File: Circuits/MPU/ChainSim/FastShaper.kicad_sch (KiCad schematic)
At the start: 34 parts, among them U20 ADA4805-2ARMZ, U21 ADA4805-2ARMZ

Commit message: sim snapshot
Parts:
- renumbered C79 to C1, C88 to C10, C89 to C11, C90 to C12, C80 to C2, C81 to C3, C82 to C4, C83 to C5, C84 to C6, C85 to C7, C86 to C8, C87 to C9, D19 to D1, D20 to D2, R112 to R10, R113 to R11, R114 to R12, R115 to R13, R116 to R14, R117 to R15, R118 to R16, R119 to R17, R120 to R18, R121 to R19, R122 to R20, R105 to R3, R106 to R4, R107 to R5, R108 to R6, R109 to R7, R110 to R8, R111 to R9, U20 to U3, U21 to U4

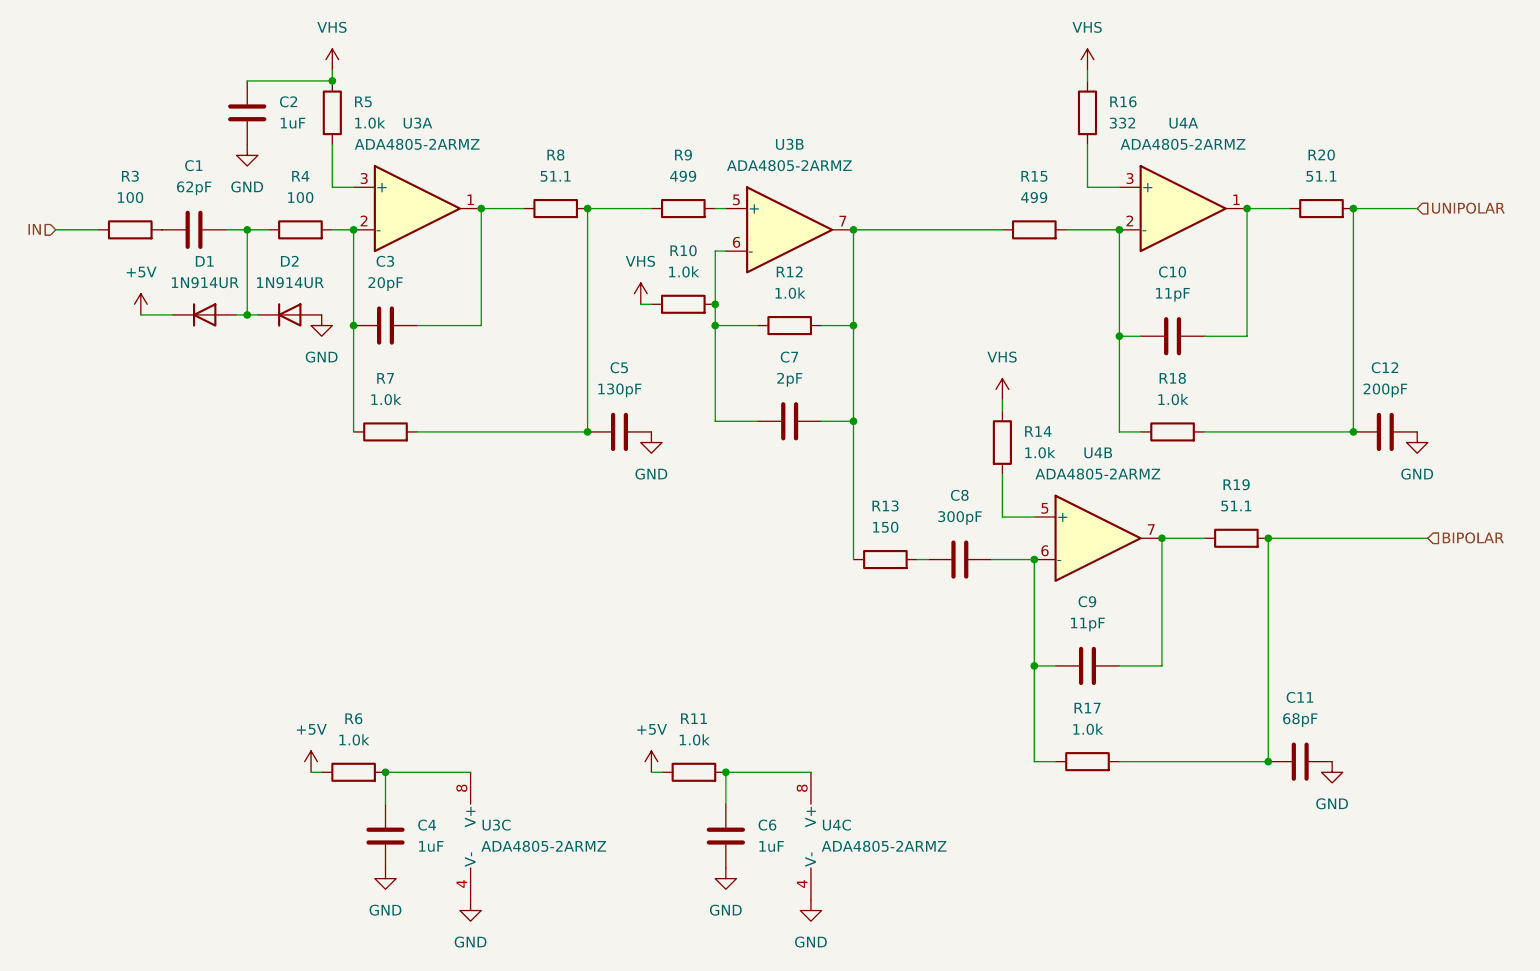
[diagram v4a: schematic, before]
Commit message: exported netlist works with ngspice
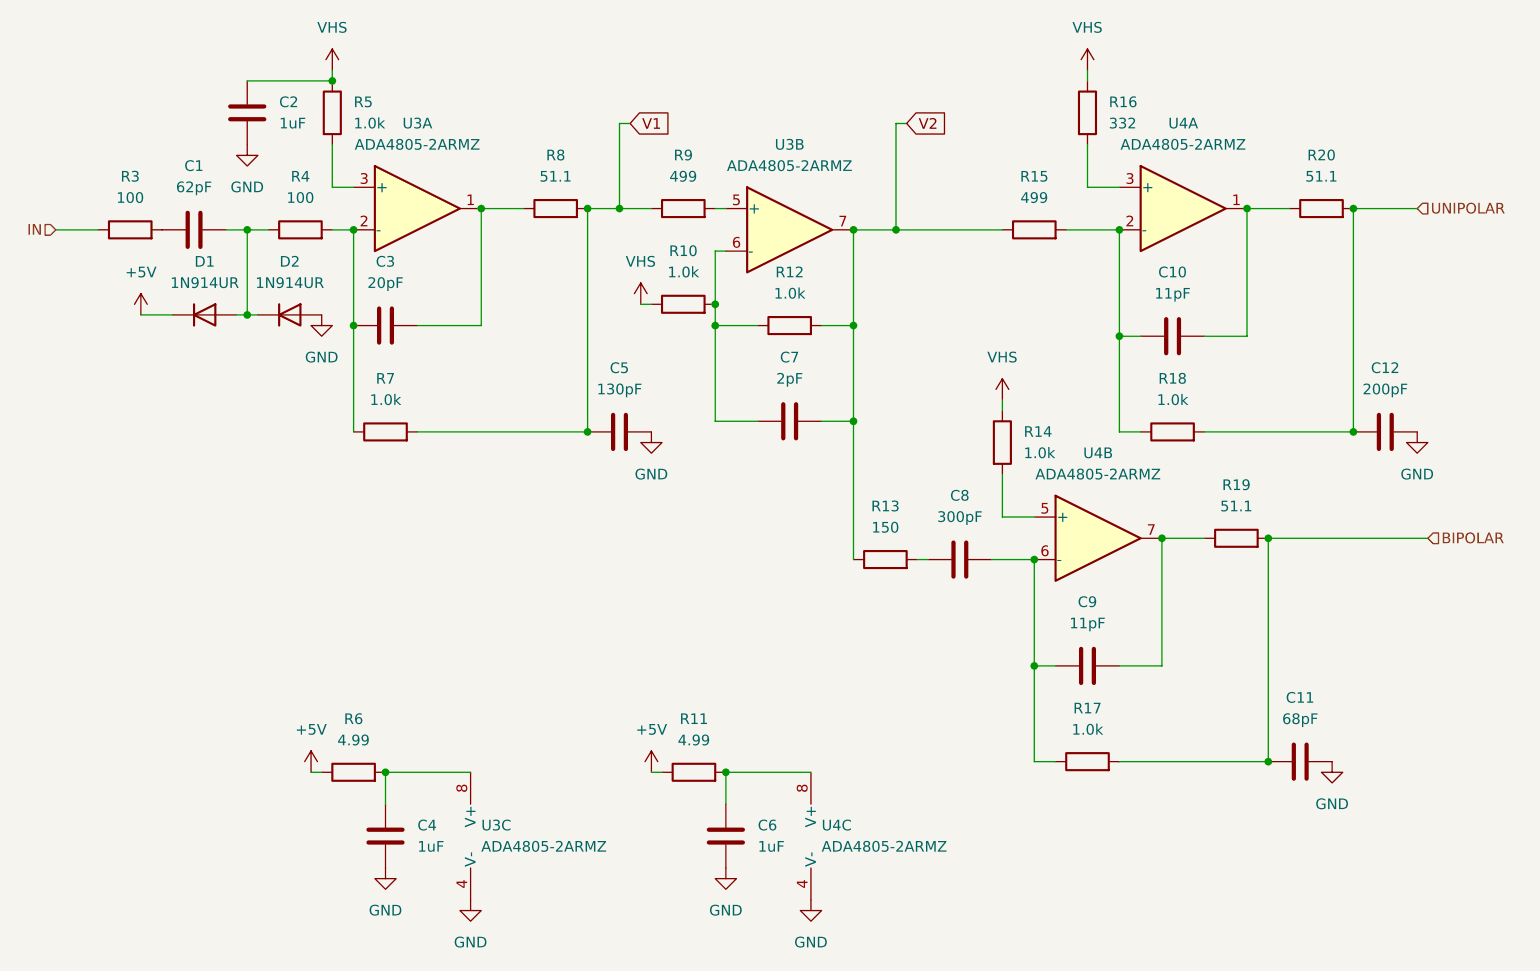
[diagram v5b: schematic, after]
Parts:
- R11, R6: value 1.0k -> 4.99
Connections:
- net V2: now reaches C7.2, R12.2, R13.1, R15.1, U3.7
- net V1: now reaches C5.1, R7.2, R8.2, R9.1
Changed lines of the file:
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@@
 	)
 	(junction
+		(at 142.24 68.58)
+		(diameter 0)
+		(color 0 0 0 0)
+	)
+	(junction
 		(at 120.65 77.47)
 		(diameter 0)
@@
 		(color 0 0 0 0)
 	)
+	(junction
+		(at 109.22 66.04)
+		(diameter 0)
+		(color 0 0 0 0)
+	)
 	(wire
 		(pts
@@
 	(wire
 		(pts
+			(xy 142.24 68.58) (xy 154.94 68.58)
+		)
+		(stroke
+			(width 0)
+			(type default)
+		)
+	)
+	(wire
+		(pts
 			(xy 165.1 49.53) (xy 165.1 50.8)
 		)
@@
 	(wire
 		(pts
-			(xy 137.16 68.58) (xy 154.94 68.58)
+			(xy 137.16 68.58) (xy 142.24 68.58)
 		)
 		(stroke
@@
 	(wire
 		(pts
+			(xy 109.22 66.04) (xy 113.03 66.04)
+		)
+		(stroke
+			(width 0)
+			(type default)
+		)
+	)
+	(wire
+		(pts
 			(xy 168.91 120.65) (xy 173.99 120.65)
 		)
@@
 	(wire
 		(pts
-			(xy 105.41 66.04) (xy 113.03 66.04)
+			(xy 105.41 66.04) (xy 109.22 66.04)
 		)
 		(stroke
@@
 	(wire
 		(pts
+			(xy 109.22 55.88) (xy 109.22 66.04)
+		)
+		(stroke
+			(width 0)
+			(type default)
+		)
+	)
+	(wire
+		(pts
+			(xy 110.49 55.88) (xy 109.22 55.88)
+		)
+		(stroke
+			(width 0)
+			(type default)
+		)
+	)
+	(wire
+		(pts
+			(xy 143.51 55.88) (xy 142.24 55.88)
+		)
+		(stroke
+			(width 0)
+			(type default)
+		)
+	)
+	(wire
+		(pts
 			(xy 120.65 91.44) (xy 120.65 80.01)
 		)
@@
 	(wire
 		(pts
+			(xy 142.24 55.88) (xy 142.24 68.58)
+		)
+		(stroke
+			(width 0)
+			(type default)
+		)
+	)
+	(wire
+		(pts
 			(xy 179.07 81.28) (xy 184.15 81.28)
 		)
@@
 		)
 	)
+	(global_label "V1"
+		(shape input)
+		(at 110.49 55.88 0)
+		(fields_autoplaced yes)
+		(effects
+			(font
+				(size 1.27 1.27)
+			)
+			(justify left)
+		)
+		(property "Intersheetrefs" "${INTERSHEET_REFS}"
+			(at 115.7733 55.88 0)
+			(effects
+				(font
+					(size 1.27 1.27)
+				)
+				(justify left)
+				(hide yes)
+			)
+		)
+	)
+	(global_label "V2"
+		(shape input)
+		(at 143.51 55.88 0)
+		(fields_autoplaced yes)
+		(effects
+			(font
+				(size 1.27 1.27)
+			)
+			(justify left)
+		)
+		(property "Intersheetrefs" "${INTERSHEET_REFS}"
+			(at 148.7933 55.88 0)
+			(effects
+				(font
+					(size 1.27 1.27)
+				)
+				(justify left)
+				(hide yes)
+			)
+		)
+	)
 	(hierarchical_label "UNIPOLAR"
 		(shape input)
@@
 			)
 		)
-		(property "Sim.Pins" "1=A 2=K"
+		(property "Sim.Pins" "1=K 2=A"
 			(at 69.85 78.74 0)
 			(effects
@@
 			)
 		)
-		(property "Sim.Pins" "1=A 2=K"
+		(property "Sim.Pins" "1=K 2=A"
 			(at 59.69 78.74 0)
 			(effects
@@
 			)
 		)
-		(property "Value" "1.0k"
+		(property "Value" "4.99"
 			(at 77.47 129.54 90)
 			(effects
@@
 			)
 		)
-		(property "Value" "1.0k"
+		(property "Value" "4.99"
 			(at 118.11 129.54 90)
 			(effects

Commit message: balance fast shaper
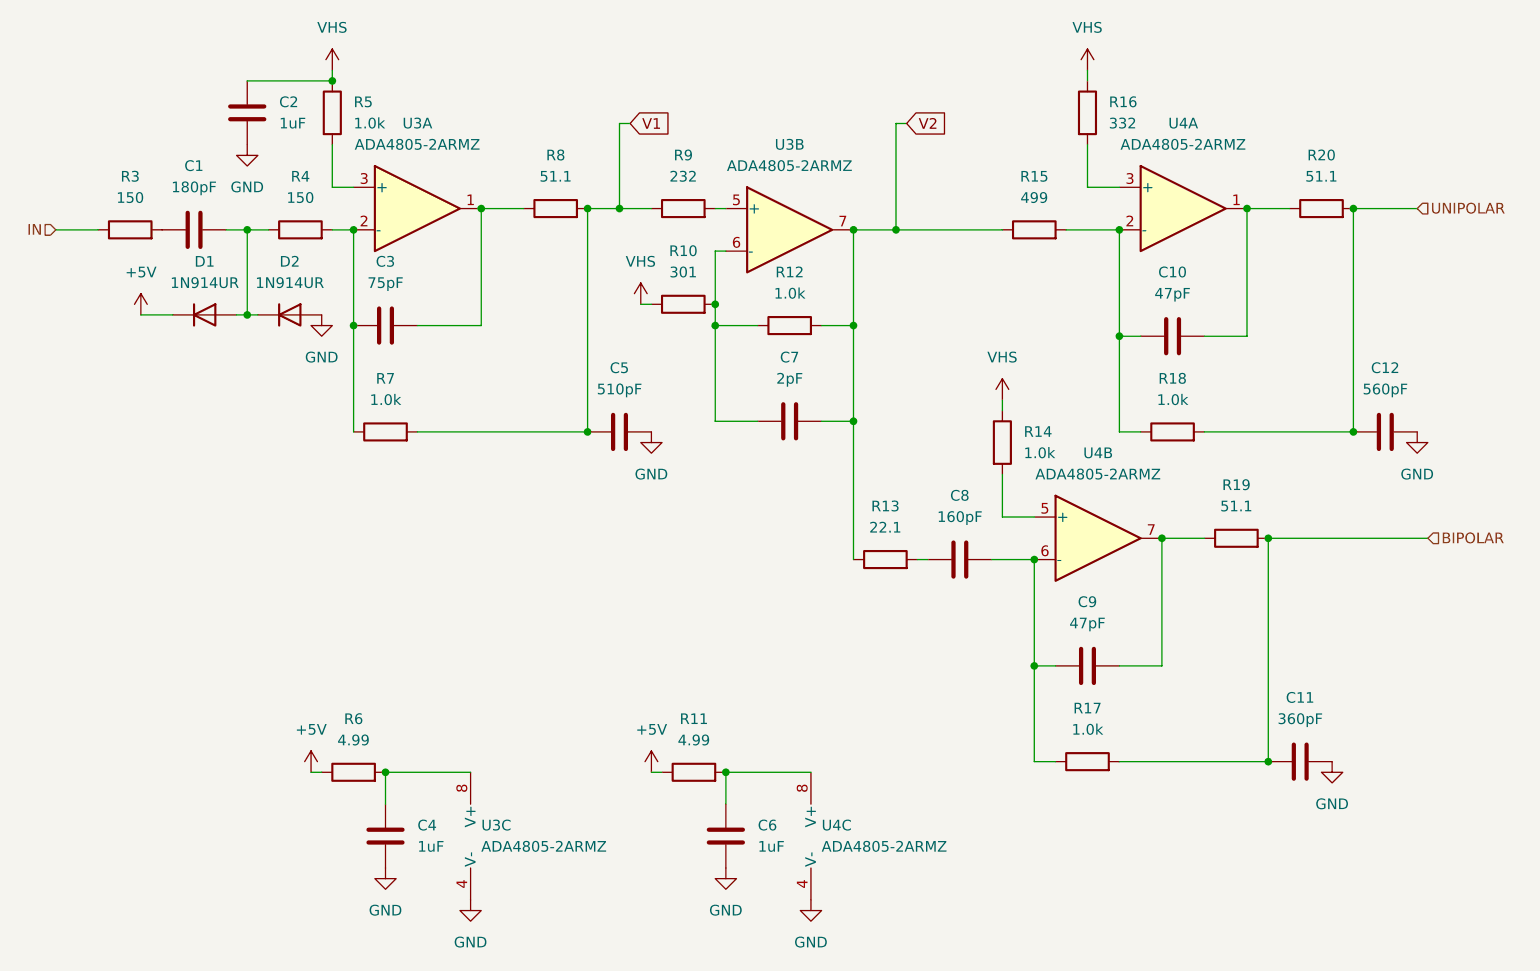
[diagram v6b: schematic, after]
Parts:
- C1: value 62pF -> 180pF
- C10, C9: value 11pF -> 47pF
- C11: value 68pF -> 360pF
- C12: value 200pF -> 560pF
- C3: value 20pF -> 75pF
- C5: value 130pF -> 510pF
- C8: value 300pF -> 160pF
- R10: value 1.0k -> 301
- R13: value 150 -> 22.1
- R3, R4: value 100 -> 150
- R9: value 499 -> 232
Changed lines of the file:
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@@
 			)
 		)
-		(property "Value" "11pF"
+		(property "Value" "47pF"
 			(at 175.26 76.2 90)
 			(effects
@@
 			)
 		)
-		(property "Value" "499"
+		(property "Value" "232"
 			(at 116.84 62.23 90)
 			(effects
@@
 			)
 		)
-		(property "Value" "68pF"
+		(property "Value" "360pF"
 			(at 190.5 127 90)
 			(effects
@@
 			)
 		)
-		(property "Value" "11pF"
+		(property "Value" "47pF"
 			(at 165.1 115.57 90)
 			(effects
@@
 			)
 		)
-		(property "Value" "100"
+		(property "Value" "150"
 			(at 71.12 64.77 90)
 			(effects
@@
 			)
 		)
-		(property "Value" "100"
+		(property "Value" "150"
 			(at 50.8 64.77 90)
 			(effects
@@
 			)
 		)
-		(property "Value" "1.0k"
+		(property "Value" "301"
 			(at 116.84 73.66 90)
 			(effects
@@
 			)
 		)
-		(property "Value" "150"
+		(property "Value" "22.1"
 			(at 140.97 104.14 90)
 			(effects
@@
 			)
 		)
-		(property "Value" "200pF"
+		(property "Value" "560pF"
 			(at 200.66 87.63 90)
 			(effects
@@
 			)
 		)
-		(property "Value" "300pF"
+		(property "Value" "160pF"
 			(at 149.86 102.87 90)
 			(effects
@@
 			)
 		)
-		(property "Value" "130pF"
+		(property "Value" "510pF"
 			(at 109.22 87.63 90)
 			(effects
@@
 			)
 		)
-		(property "Value" "20pF"
+		(property "Value" "75pF"
 			(at 81.28 74.93 90)
 			(effects
@@
 			)
 		)
-		(property "Value" "62pF"
+		(property "Value" "180pF"
 			(at 58.42 63.5 90)
 			(effects
